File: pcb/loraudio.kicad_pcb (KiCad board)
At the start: 2 copper layers, 70 x 50 mm, 0 parts

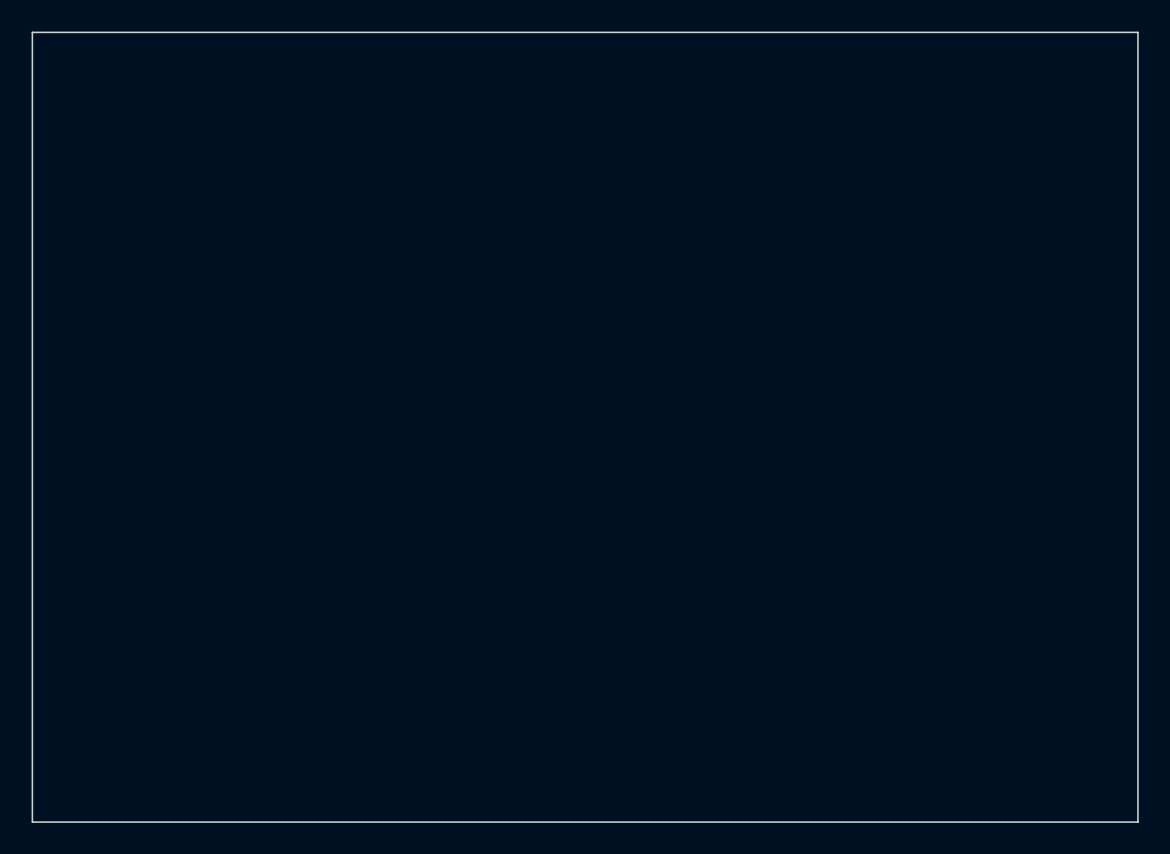
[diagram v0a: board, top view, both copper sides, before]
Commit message: Add mounting holes and split KiCad generator into library + board script
Co-Authored-By: Claude Opus 4.6 <noreply@anthropic.com>
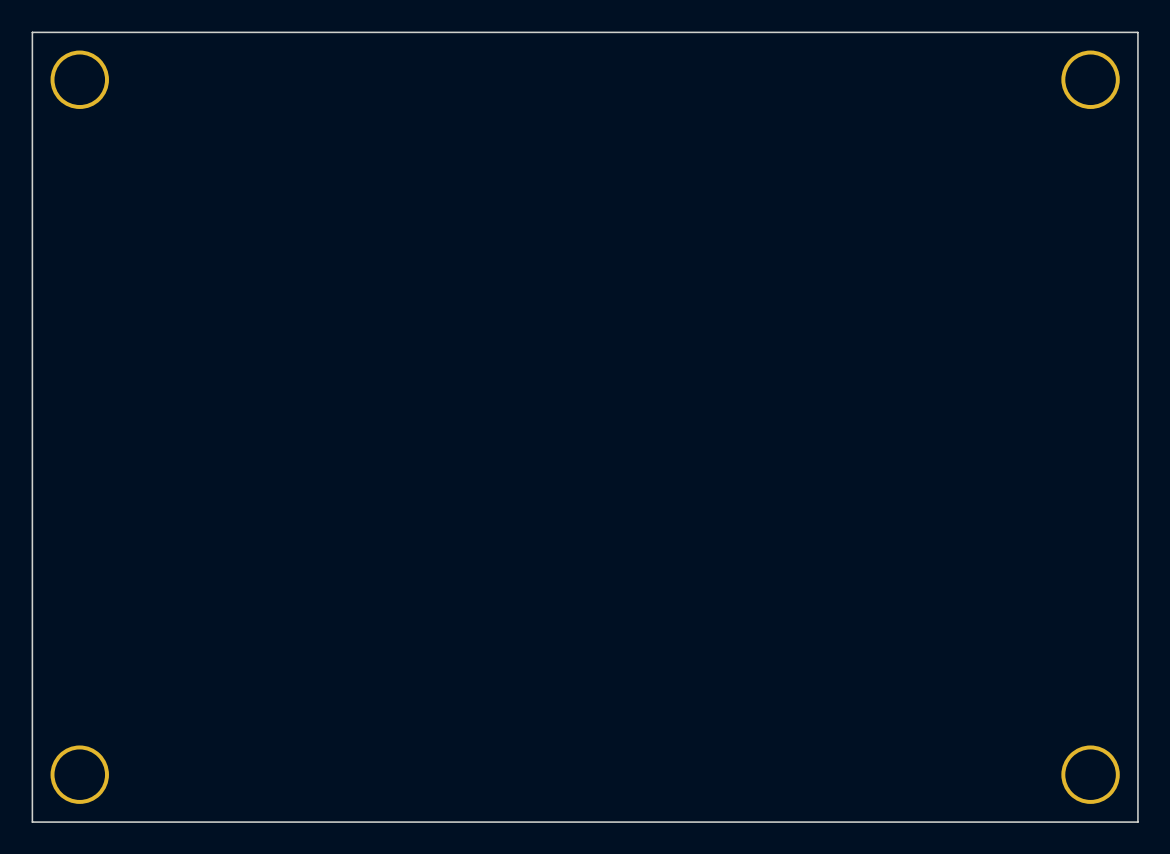
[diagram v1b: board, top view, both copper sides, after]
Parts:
- added ?: , MountingHole_3.2mm, F.Cu at (116.0, 116.0)
- added ?: , MountingHole_3.2mm, F.Cu at (116.0, 160.0)
- added ?: , MountingHole_3.2mm, F.Cu at (180.0, 116.0)
- added ?: , MountingHole_3.2mm, F.Cu at (180.0, 160.0)
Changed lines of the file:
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@@
   (net 0 "")
   (gr_rect (start 113 113) (end 183 163) (stroke (width 0.1) (type solid)) (fill none) (layer "Edge.Cuts"))
+  (footprint "MountingHole_3.2mm"
+    (layer "F.Cu")
+    (at 116 116)
+    (attr exclude_from_pos_files exclude_from_bom)
+    (fp_text reference "" (at 0 0) (layer "F.SilkS") hide
+      (effects (font (size 1 1) (thickness 0.15)))
+    )
+    (pad "" np_thru_hole circle
+      (at 0 0)
+      (size 3.7 3.7)
+      (drill 3.2)
+      (layers *.Cu *.Mask)
+    )
+  )
+  (footprint "MountingHole_3.2mm"
+    (layer "F.Cu")
+    (at 116 160)
+    (attr exclude_from_pos_files exclude_from_bom)
+    (fp_text reference "" (at 0 0) (layer "F.SilkS") hide
+      (effects (font (size 1 1) (thickness 0.15)))
+    )
+    (pad "" np_thru_hole circle
+      (at 0 0)
+      (size 3.7 3.7)
+      (drill 3.2)
+      (layers *.Cu *.Mask)
+    )
+  )
+  (footprint "MountingHole_3.2mm"
+    (layer "F.Cu")
+    (at 180 116)
+    (attr exclude_from_pos_files exclude_from_bom)
+    (fp_text reference "" (at 0 0) (layer "F.SilkS") hide
+      (effects (font (size 1 1) (thickness 0.15)))
+    )
+    (pad "" np_thru_hole circle
+      (at 0 0)
+      (size 3.7 3.7)
+      (drill 3.2)
+      (layers *.Cu *.Mask)
+    )
+  )
+  (footprint "MountingHole_3.2mm"
+    (layer "F.Cu")
+    (at 180 160)
+    (attr exclude_from_pos_files exclude_from_bom)
+    (fp_text reference "" (at 0 0) (layer "F.SilkS") hide
+      (effects (font (size 1 1) (thickness 0.15)))
+    )
+    (pad "" np_thru_hole circle
+      (at 0 0)
+      (size 3.7 3.7)
+      (drill 3.2)
+      (layers *.Cu *.Mask)
+    )
+  )
 )

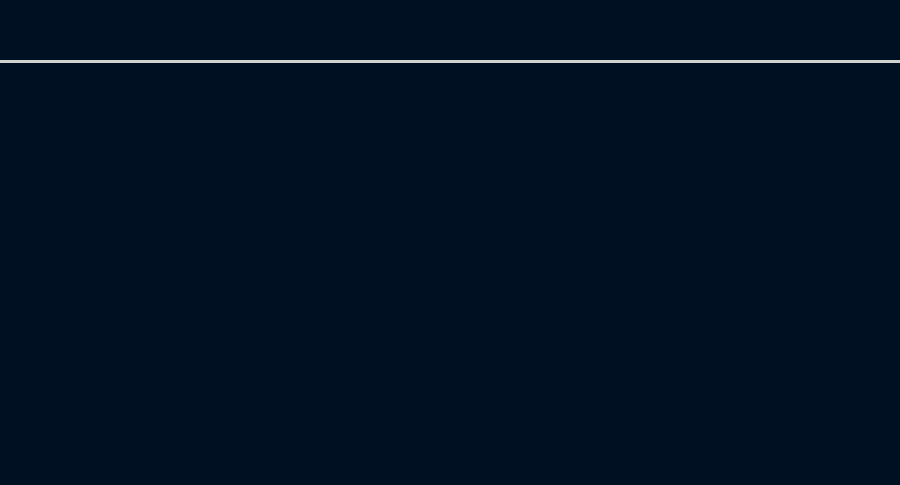
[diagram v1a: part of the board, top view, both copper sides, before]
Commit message: Add JST-PH through-hole connector for speaker
Co-Authored-By: Claude Opus 4.6 <noreply@anthropic.com>
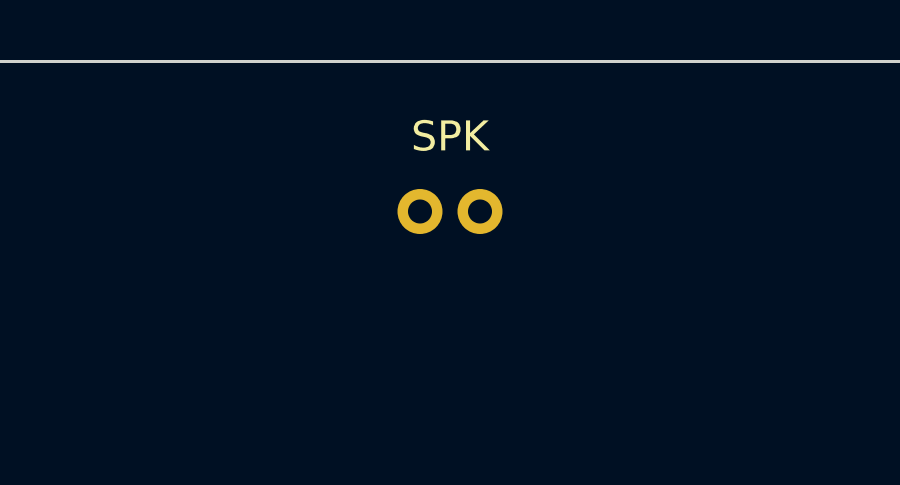
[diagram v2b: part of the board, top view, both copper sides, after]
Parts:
- added SPK: , JST_PH_B2B, F.Cu at (148.0, 118.0)
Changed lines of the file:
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@@
+    )
+  )
+  (footprint "JST_PH_B2B"
+    (layer "F.Cu")
+    (at 148 118)
+    (fp_text reference "SPK" (at 0 -2.5) (layer "F.SilkS")
+      (effects (font (size 1 1) (thickness 0.15)))
+    )
+    (pad "+" thru_hole circle
+      (at -1.0 0)
+      (size 1.5 1.5)
+      (drill 0.8)
+      (layers *.Cu *.Mask)
+    )
+    (pad "-" thru_hole circle
+      (at 1.0 0)
+      (size 1.5 1.5)
+      (drill 0.8)
+      (layers *.Cu *.Mask)
     )
   )

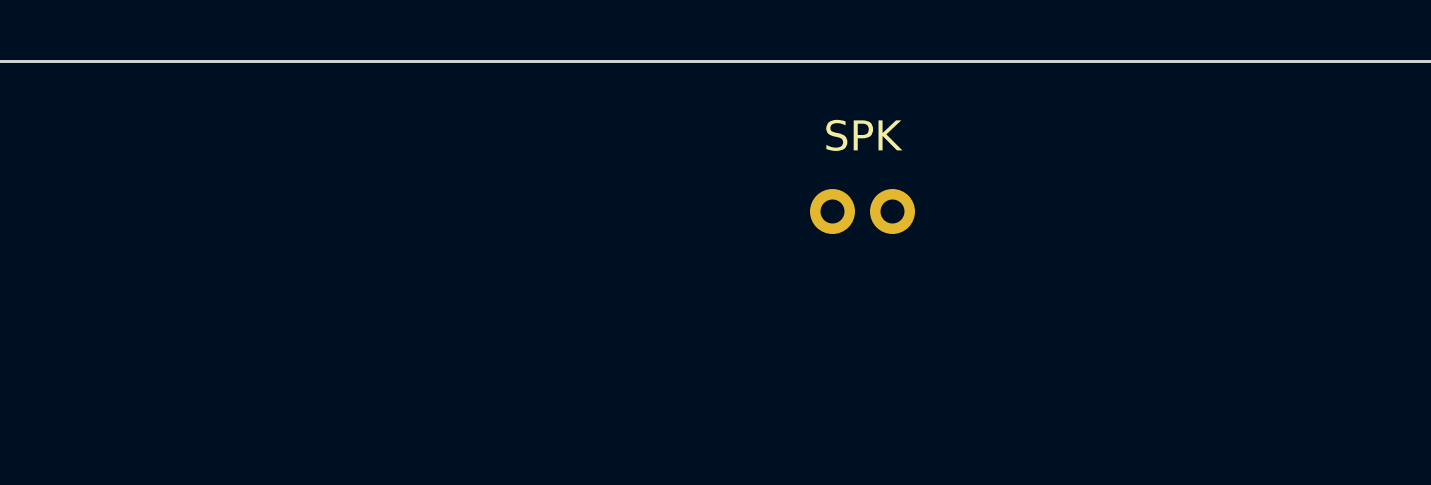
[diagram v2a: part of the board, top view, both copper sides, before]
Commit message: Add JST connectors for battery, PA power, PTT and power switch
JST-PH 2.0mm for SPK, BAT, PTT, PWR; JST-SH 1.25mm for PA.
All through-hole, single row along top edge.

Co-Authored-By: Claude Opus 4.6 <noreply@anthropic.com>
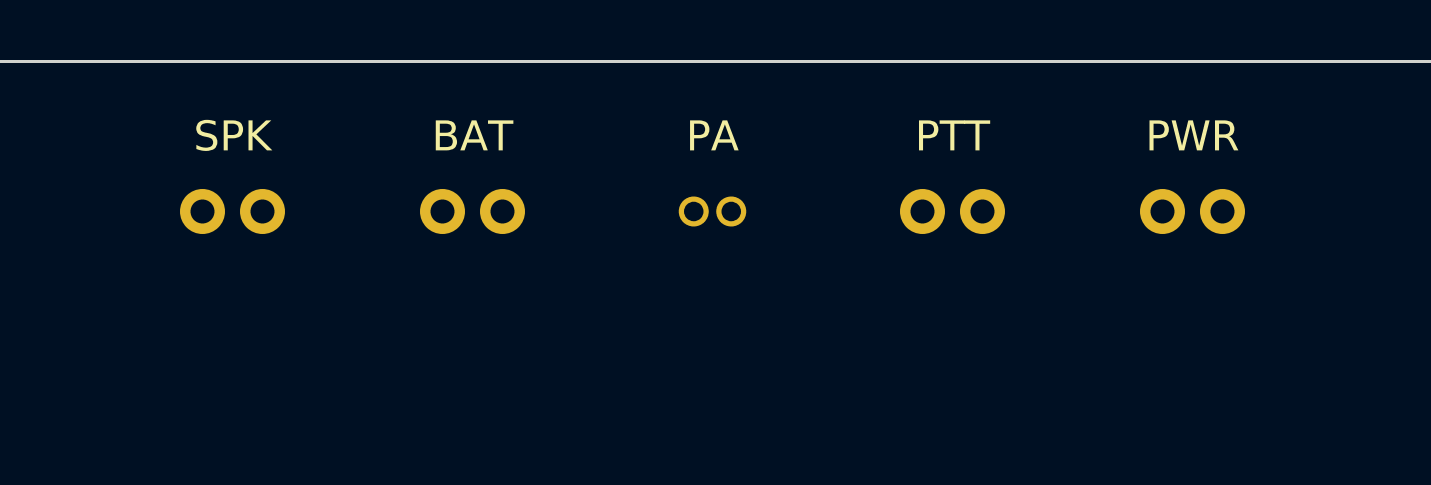
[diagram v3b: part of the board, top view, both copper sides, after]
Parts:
- added BAT: , JST_PH_B2B, F.Cu at (135.0, 118.0)
- added PA: , JST_SH_B2B, F.Cu at (143.0, 118.0)
- added PTT: , JST_PH_B2B, F.Cu at (151.0, 118.0)
- added PWR: , JST_PH_B2B, F.Cu at (159.0, 118.0)
- moved SPK 21.0 mm to (127.0, 118.0)
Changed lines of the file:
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@@
   (footprint "JST_PH_B2B"
     (layer "F.Cu")
-    (at 148 118)
+    (at 127 118)
     (fp_text reference "SPK" (at 0 -2.5) (layer "F.SilkS")
       (effects (font (size 1 1) (thickness 0.15)))
@@
       (at 1.0 0)
       (size 1.5 1.5)
+      (drill 0.8)
+      (layers *.Cu *.Mask)
+    )
+  )
+  (footprint "JST_PH_B2B"
+    (layer "F.Cu")
+    (at 135 118)
+    (fp_text reference "BAT" (at 0 -2.5) (layer "F.SilkS")
+      (effects (font (size 1 1) (thickness 0.15)))
+    )
+    (pad "+" thru_hole circle
+      (at -1.0 0)
+      (size 1.5 1.5)
+      (drill 0.8)
+      (layers *.Cu *.Mask)
+    )
+    (pad "-" thru_hole circle
+      (at 1.0 0)
+      (size 1.5 1.5)
+      (drill 0.8)
+      (layers *.Cu *.Mask)
+    )
+  )
+  (footprint "JST_SH_B2B"
+    (layer "F.Cu")
+    (at 143 118)
+    (fp_text reference "PA" (at 0 -2.5) (layer "F.SilkS")
+      (effects (font (size 1 1) (thickness 0.15)))
+    )
+    (pad "+" thru_hole circle
+      (at -0.625 0)
+      (size 1.0 1.0)
+      (drill 0.65)
+      (layers *.Cu *.Mask)
+    )
+    (pad "-" thru_hole circle
+      (at 0.625 0)
+      (size 1.0 1.0)
+      (drill 0.65)
+      (layers *.Cu *.Mask)
+    )
+  )
+  (footprint "JST_PH_B2B"
+    (layer "F.Cu")
+    (at 151 118)
+    (fp_text reference "PTT" (at 0 -2.5) (layer "F.SilkS")
+      (effects (font (size 1 1) (thickness 0.15)))
+    )
+    (pad "1" thru_hole circle
+      (at -1.0 0)
+      (size 1.5 1.5)
+      (drill 0.8)
+      (layers *.Cu *.Mask)
+    )
+    (pad "2" thru_hole circle
+      (at 1.0 0)
+      (size 1.5 1.5)
+      (drill 0.8)
+      (layers *.Cu *.Mask)
+    )
+  )
+  (footprint "JST_PH_B2B"
+    (layer "F.Cu")
+    (at 159 118)
+    (fp_text reference "PWR" (at 0 -2.5) (layer "F.SilkS")
+      (effects (font (size 1 1) (thickness 0.15)))
+    )
+    (pad "1" thru_hole circle
+      (at -1.0 0)
+      (size 1.5 1.5)
+      (drill 0.8)
+      (layers *.Cu *.Mask)
+    )
+    (pad "2" thru_hole circle
+      (at 1.0 0)
+      (size 1.5 1.5)

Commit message: Add mic header and generic pin header to KiCad generator
5-pin 2.54mm header for MAX9814 mic board, centered on bottom edge.
Also adds add_header() method for standard pitch pin headers.

Co-Authored-By: Claude Opus 4.6 <noreply@anthropic.com>
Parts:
- added MIC: , PinHeader_1x5_P2.54mm, F.Cu at (148.0, 158.0)
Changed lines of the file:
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@@
+    )
+  )
+  (footprint "PinHeader_1x5_P2.54mm"
+    (layer "F.Cu")
+    (at 148.0 158)
+    (fp_text reference "MIC" (at 0 -2.5) (layer "F.SilkS")
+      (effects (font (size 1 1) (thickness 0.15)))
+    )
+    (pad "OUT" thru_hole circle
+      (at -5.08 0)
+      (size 1.7 1.7)
+      (drill 1.0)
+      (layers *.Cu *.Mask)
+    )
+    (pad "GND" thru_hole circle
+      (at -2.54 0)
+      (size 1.7 1.7)
+      (drill 1.0)
+      (layers *.Cu *.Mask)
+    )
+    (pad "VDD" thru_hole circle
+      (at 0.0 0)
+      (size 1.7 1.7)
+      (drill 1.0)
+      (layers *.Cu *.Mask)
+    )
+    (pad "AR" thru_hole circle
+      (at 2.54 0)
+      (size 1.7 1.7)
+      (drill 1.0)
+      (layers *.Cu *.Mask)
+    )
+    (pad "GAIN" thru_hole circle
+      (at 5.08 0)
+      (size 1.7 1.7)
+      (drill 1.0)
+      (layers *.Cu *.Mask)
     )
   )

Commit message: Add speaker amp header to bottom edge
7-pin 2.54mm header for MAX98357A, left of centered mic header.

Co-Authored-By: Claude Opus 4.6 <noreply@anthropic.com>
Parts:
- added AMP: , PinHeader_1x7_P2.54mm, F.Cu at (128.0, 158.0)
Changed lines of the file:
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@@
+    )
+  )
+  (footprint "PinHeader_1x7_P2.54mm"
+    (layer "F.Cu")
+    (at 128 158)
+    (fp_text reference "AMP" (at 0 -2.5) (layer "F.SilkS")
+      (effects (font (size 1 1) (thickness 0.15)))
+    )
+    (pad "Vin" thru_hole circle
+      (at -7.62 0)
+      (size 1.7 1.7)
+      (drill 1.0)
+      (layers *.Cu *.Mask)
+    )
+    (pad "GND" thru_hole circle
+      (at -5.08 0)
+      (size 1.7 1.7)
+      (drill 1.0)
+      (layers *.Cu *.Mask)
+    )
+    (pad "SD" thru_hole circle
+      (at -2.54 0)
+      (size 1.7 1.7)
+      (drill 1.0)
+      (layers *.Cu *.Mask)
+    )
+    (pad "GAIN" thru_hole circle
+      (at 0.0 0)
+      (size 1.7 1.7)
+      (drill 1.0)
+      (layers *.Cu *.Mask)
+    )
+    (pad "DIN" thru_hole circle
+      (at 2.54 0)
+      (size 1.7 1.7)
+      (drill 1.0)
+      (layers *.Cu *.Mask)
+    )
+    (pad "BCLK" thru_hole circle
+      (at 5.079999999999999 0)
+      (size 1.7 1.7)
+      (drill 1.0)
+      (layers *.Cu *.Mask)
+    )
+    (pad "LRC" thru_hole circle
+      (at 7.62 0)
+      (size 1.7 1.7)
+      (drill 1.0)
+      (layers *.Cu *.Mask)
     )
   )

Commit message: Add net support to KiCad generator for autorouting
Pads now carry net assignments (GND, VBAT, I2S_BCLK, etc.)
so Freerouting can automatically route traces between them.

Co-Authored-By: Claude Opus 4.6 <noreply@anthropic.com>
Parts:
- removed ? (x4): , MountingHole_3.2mm
- added H1: , MountingHole_3.2mm, F.Cu at (116.0, 116.0)
- added H2: , MountingHole_3.2mm, F.Cu at (116.0, 160.0)
- added H3: , MountingHole_3.2mm, F.Cu at (180.0, 116.0)
- added H4: , MountingHole_3.2mm, F.Cu at (180.0, 160.0)
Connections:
- AMP pad BCLK: (no net) -> I2S_BCLK
- AMP pad DIN: (no net) -> I2S_DIN
- AMP pad GND: (no net) -> GND
- AMP pad LRC: (no net) -> I2S_LRC
- AMP pad Vin: (no net) -> VBAT
- BAT pad +: (no net) -> VBAT
- BAT pad -: (no net) -> GND
- MIC pad GND: (no net) -> GND
- MIC pad OUT: (no net) -> MIC_OUT
- MIC pad VDD: (no net) -> VBAT
- PA pad +: (no net) -> VBAT
- PA pad -: (no net) -> GND
- PTT pad 1: (no net) -> PTT
- PTT pad 2: (no net) -> GND
- PWR pad 1: (no net) -> VBAT
- PWR pad 2: (no net) -> PWR_SW
- SPK pad +: (no net) -> SPK+
- SPK pad -: (no net) -> GND
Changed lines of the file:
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@@
   )
   (net 0 "")
+  (net 1 "SPK+")
+  (net 2 "GND")
+  (net 3 "VBAT")
+  (net 4 "PTT")
+  (net 5 "PWR_SW")
+  (net 6 "MIC_OUT")
+  (net 7 "I2S_DIN")
+  (net 8 "I2S_BCLK")
+  (net 9 "I2S_LRC")
   (gr_rect (start 113 113) (end 183 163) (stroke (width 0.1) (type solid)) (fill none) (layer "Edge.Cuts"))
   (footprint "MountingHole_3.2mm"
@@
     (at 116 116)
     (attr exclude_from_pos_files exclude_from_bom)
-    (fp_text reference "" (at 0 0) (layer "F.SilkS") hide
+    (fp_text reference "H1" (at 0 0) (layer "F.SilkS") hide
       (effects (font (size 1 1) (thickness 0.15)))
     )
@@
     (at 116 160)
     (attr exclude_from_pos_files exclude_from_bom)
-    (fp_text reference "" (at 0 0) (layer "F.SilkS") hide
+    (fp_text reference "H2" (at 0 0) (layer "F.SilkS") hide
       (effects (font (size 1 1) (thickness 0.15)))
     )
@@
     (at 180 116)
     (attr exclude_from_pos_files exclude_from_bom)
-    (fp_text reference "" (at 0 0) (layer "F.SilkS") hide
+    (fp_text reference "H3" (at 0 0) (layer "F.SilkS") hide
       (effects (font (size 1 1) (thickness 0.15)))
     )
@@
     (at 180 160)
     (attr exclude_from_pos_files exclude_from_bom)
-    (fp_text reference "" (at 0 0) (layer "F.SilkS") hide
+    (fp_text reference "H4" (at 0 0) (layer "F.SilkS") hide
       (effects (font (size 1 1) (thickness 0.15)))
     )
@@
       (drill 0.8)
       (layers *.Cu *.Mask)
+      (net 1 "SPK+")
     )
     (pad "-" thru_hole circle
@@
       (drill 0.8)
       (layers *.Cu *.Mask)
+      (net 2 "GND")
     )
   )
@@
       (drill 0.8)
       (layers *.Cu *.Mask)
+      (net 3 "VBAT")
     )
     (pad "-" thru_hole circle
@@
       (drill 0.8)
       (layers *.Cu *.Mask)
+      (net 2 "GND")
     )
   )
@@
       (drill 0.65)
       (layers *.Cu *.Mask)
+      (net 3 "VBAT")
     )
     (pad "-" thru_hole circle
@@
       (drill 0.65)
       (layers *.Cu *.Mask)
+      (net 2 "GND")
     )
   )
@@
       (drill 0.8)
       (layers *.Cu *.Mask)
+      (net 4 "PTT")
     )
     (pad "2" thru_hole circle
@@
       (drill 0.8)
       (layers *.Cu *.Mask)
+      (net 2 "GND")
     )
   )
@@
       (drill 0.8)
       (layers *.Cu *.Mask)
+      (net 3 "VBAT")
     )
     (pad "2" thru_hole circle
@@
       (drill 0.8)
       (layers *.Cu *.Mask)
+      (net 5 "PWR_SW")
     )
   )
@@
       (drill 1.0)
       (layers *.Cu *.Mask)
+      (net 6 "MIC_OUT")
     )
     (pad "GND" thru_hole circle
@@
       (drill 1.0)
       (layers *.Cu *.Mask)
+      (net 2 "GND")
     )
     (pad "VDD" thru_hole circle
@@
       (drill 1.0)
       (layers *.Cu *.Mask)
+      (net 3 "VBAT")
     )
     (pad "AR" thru_hole circle
@@
       (drill 1.0)
       (layers *.Cu *.Mask)
+      (net 3 "VBAT")
     )
     (pad "GND" thru_hole circle
@@
       (drill 1.0)
       (layers *.Cu *.Mask)
+      (net 2 "GND")
     )
     (pad "SD" thru_hole circle
@@
       (drill 1.0)
       (layers *.Cu *.Mask)
+      (net 7 "I2S_DIN")
     )
     (pad "BCLK" thru_hole circle
@@
       (drill 1.0)
       (layers *.Cu *.Mask)
+      (net 8 "I2S_BCLK")
     )
     (pad "LRC" thru_hole circle
@@
       (drill 1.0)
       (layers *.Cu *.Mask)
-    )
-  )
+      (net 9 "I2S_LRC")
+    )
+  )
